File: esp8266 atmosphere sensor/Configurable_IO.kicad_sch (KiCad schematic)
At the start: 5 parts, among them J14 Conn_01x03

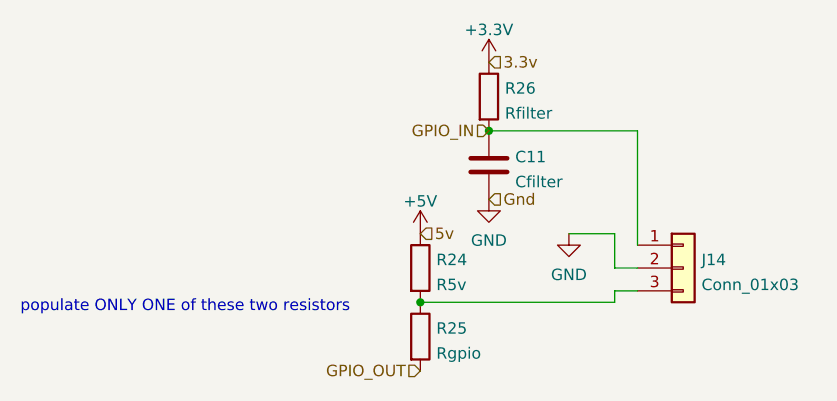
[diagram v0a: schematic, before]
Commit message: updated footprints
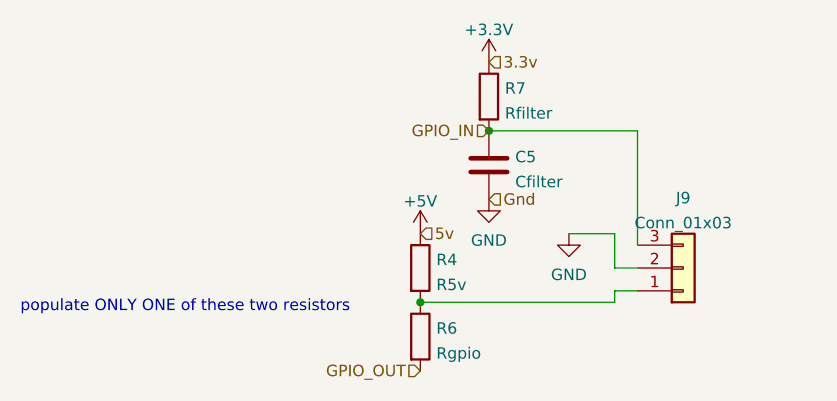
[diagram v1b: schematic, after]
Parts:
- renumbered C11 to C5, J14 to J9, R24 to R4, R25 to R6, R26 to R7
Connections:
- net GPIO_IN: now also J9.3 (Pin_3); no longer J9.1 (Pin_1)
- net at R4.2, R6.1: now also J9.1 (Pin_1); no longer J9.3 (Pin_3)
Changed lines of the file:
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@@
   (symbol (lib_id "power:GND") (at 82.55 60.96 0)
     (in_bom yes) (on_board yes) (fields_autoplaced)
-    (property "Reference" "#PWR0171" (id 0) (at 82.55 67.31 0)
+    (property "Reference" "#PWR0151" (id 0) (at 82.55 67.31 0)
       (effects (font (size 1.27 1.27)) hide)
     )
@@
   (symbol (lib_id "Device:R") (at 74.93 68.58 0)
     (in_bom yes) (on_board yes) (fields_autoplaced)
-    (property "Reference" "R24" (id 0) (at 76.708 67.6715 0)
+    (property "Reference" "R4" (id 0) (at 76.708 67.6715 0)
       (effects (font (size 1.27 1.27)) (justify left))
     )
@@
     (pin "2")
   )
-  (symbol (lib_id "Connector_Generic:Conn_01x03") (at 104.14 68.58 0)
+  (symbol (lib_id "Connector_Generic:Conn_01x03") (at 104.14 68.58 0) (mirror x)
     (in_bom yes) (on_board yes) (fields_autoplaced)
-    (property "Reference" "J14" (id 0) (at 106.172 67.6715 0)
-      (effects (font (size 1.27 1.27)) (justify left))
-    )
-    (property "Value" "Conn_01x03" (id 1) (at 106.172 70.4466 0)
-      (effects (font (size 1.27 1.27)) (justify left))
-    )
+    (property "Reference" "J9" (id 0) (at 104.14 60.8035 0))
+    (property "Value" "Conn_01x03" (id 1) (at 104.14 63.5786 0))
     (property "Footprint" "Connector_JST:JST_PH_B3B-PH-SM4-TB_1x03-1MP_P2.00mm_Vertical" (id 2) (at 104.14 68.58 0)
       (effects (font (size 1.27 1.27)) hide)
@@
   (symbol (lib_id "power:GND") (at 91.44 64.77 0)
     (in_bom yes) (on_board yes) (fields_autoplaced)
-    (property "Reference" "#PWR0174" (id 0) (at 91.44 71.12 0)
+    (property "Reference" "#PWR0154" (id 0) (at 91.44 71.12 0)
       (effects (font (size 1.27 1.27)) hide)
     )
@@
   (symbol (lib_id "power:+3.3V") (at 82.55 45.72 0)
     (in_bom yes) (on_board yes) (fields_autoplaced)
-    (property "Reference" "#PWR0173" (id 0) (at 82.55 49.53 0)
+    (property "Reference" "#PWR0153" (id 0) (at 82.55 49.53 0)
       (effects (font (size 1.27 1.27)) hide)
     )
@@
   (symbol (lib_id "Device:C") (at 82.55 57.15 0)
     (in_bom yes) (on_board yes) (fields_autoplaced)
-    (property "Reference" "C11" (id 0) (at 85.471 56.2415 0)
+    (property "Reference" "C5" (id 0) (at 85.471 56.2415 0)
       (effects (font (size 1.27 1.27)) (justify left))
     )
@@
   (symbol (lib_id "power:+5V") (at 74.93 64.77 0)
     (in_bom yes) (on_board yes) (fields_autoplaced)
-    (property "Reference" "#PWR0172" (id 0) (at 74.93 68.58 0)
+    (property "Reference" "#PWR0152" (id 0) (at 74.93 68.58 0)
       (effects (font (size 1.27 1.27)) hide)
     )
@@
   (symbol (lib_id "Device:R") (at 82.55 49.53 0)
     (in_bom yes) (on_board yes) (fields_autoplaced)
-    (property "Reference" "R26" (id 0) (at 84.328 48.6215 0)
+    (property "Reference" "R7" (id 0) (at 84.328 48.6215 0)
       (effects (font (size 1.27 1.27)) (justify left))
     )
@@
   (symbol (lib_id "Device:R") (at 74.93 76.2 0)
     (in_bom yes) (on_board yes) (fields_autoplaced)
-    (property "Reference" "R25" (id 0) (at 76.708 75.2915 0)
+    (property "Reference" "R6" (id 0) (at 76.708 75.2915 0)
       (effects (font (size 1.27 1.27)) (justify left))
     )

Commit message: added notes for populating switch components
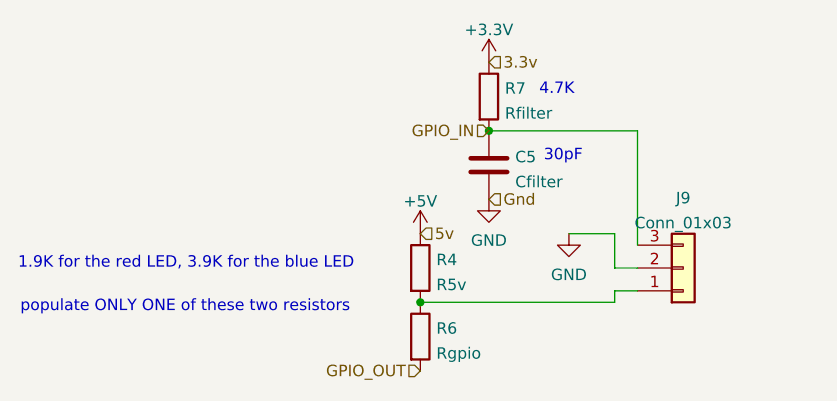
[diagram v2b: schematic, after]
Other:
- note added: "1.9K for the red LED, 3.9K for the blue LED"
- note added: "30pF"
- note added: "4.7K"
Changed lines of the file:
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@@
     (stroke (width 0) (type default) (color 0 0 0 0))
+  )
+  (text "4.7K" (at 88.138 49.53 0)
+    (effects (font (size 1.27 1.27)) (justify left bottom))
+  )
+  (text "1.9K for the red LED, 3.9K for the blue LED" (at 30.226 68.834 0)
+    (effects (font (size 1.27 1.27)) (justify left bottom))
+  )
+  (text "30pF" (at 88.646 56.896 0)
+    (effects (font (size 1.27 1.27)) (justify left bottom))
   )
   (text "populate ONLY ONE of these two resistors" (at 30.48 73.66 0)
@@
     (effects (font (size 1.27 1.27)) (justify left))
   )
-  (symbol (lib_id "power:GND") (at 82.55 60.96 0)
+  (symbol (lib_id "power:GND") (at 82.55 60.96 0) (unit 1)
     (in_bom yes) (on_board yes) (fields_autoplaced)
     (property "Reference" "#PWR0151" (id 0) (at 82.55 67.31 0)
@@
     (pin "1")
   )
-  (symbol (lib_id "Device:R") (at 74.93 68.58 0)
+  (symbol (lib_id "Device:R") (at 74.93 68.58 0) (unit 1)
     (in_bom yes) (on_board yes) (fields_autoplaced)
     (property "Reference" "R4" (id 0) (at 76.708 67.6715 0)
@@
     (pin "2")
   )
-  (symbol (lib_id "Connector_Generic:Conn_01x03") (at 104.14 68.58 0) (mirror x)
+  (symbol (lib_id "Connector_Generic:Conn_01x03") (at 104.14 68.58 0) (mirror x) (unit 1)
     (in_bom yes) (on_board yes) (fields_autoplaced)
     (property "Reference" "J9" (id 0) (at 104.14 60.8035 0))
@@
     (pin "3")
   )
-  (symbol (lib_id "power:GND") (at 91.44 64.77 0)
+  (symbol (lib_id "power:GND") (at 91.44 64.77 0) (unit 1)
     (in_bom yes) (on_board yes) (fields_autoplaced)
     (property "Reference" "#PWR0154" (id 0) (at 91.44 71.12 0)
@@
     (pin "1")
   )
-  (symbol (lib_id "power:+3.3V") (at 82.55 45.72 0)
+  (symbol (lib_id "power:+3.3V") (at 82.55 45.72 0) (unit 1)
     (in_bom yes) (on_board yes) (fields_autoplaced)
     (property "Reference" "#PWR0153" (id 0) (at 82.55 49.53 0)
@@
     (pin "1")
   )
-  (symbol (lib_id "Device:C") (at 82.55 57.15 0)
+  (symbol (lib_id "Device:C") (at 82.55 57.15 0) (unit 1)
     (in_bom yes) (on_board yes) (fields_autoplaced)
     (property "Reference" "C5" (id 0) (at 85.471 56.2415 0)
@@
     (pin "2")
   )
-  (symbol (lib_id "power:+5V") (at 74.93 64.77 0)
+  (symbol (lib_id "power:+5V") (at 74.93 64.77 0) (unit 1)
     (in_bom yes) (on_board yes) (fields_autoplaced)
     (property "Reference" "#PWR0152" (id 0) (at 74.93 68.58 0)
@@
     (pin "1")
   )
-  (symbol (lib_id "Device:R") (at 82.55 49.53 0)
+  (symbol (lib_id "Device:R") (at 82.55 49.53 0) (unit 1)
     (in_bom yes) (on_board yes) (fields_autoplaced)
     (property "Reference" "R7" (id 0) (at 84.328 48.6215 0)
@@
     (pin "2")
   )
-  (symbol (lib_id "Device:R") (at 74.93 76.2 0)
+  (symbol (lib_id "Device:R") (at 74.93 76.2 0) (unit 1)
     (in_bom yes) (on_board yes) (fields_autoplaced)
     (property "Reference" "R6" (id 0) (at 76.708 75.2915 0)

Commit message: tweaked locations for button connectors
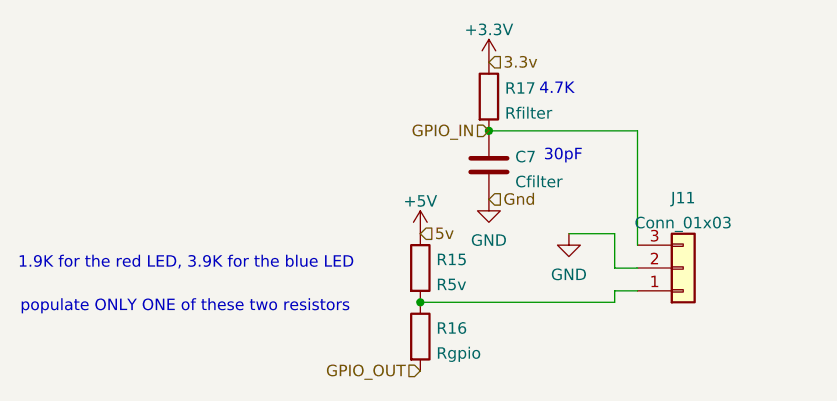
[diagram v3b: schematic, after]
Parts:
- renumbered C5 to C7, J9 to J11, R4 to R15, R6 to R16, R7 to R17
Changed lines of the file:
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@@
     (effects (font (size 1.27 1.27)) (justify left))
   )
-  (symbol (lib_id "power:GND") (at 82.55 60.96 0) (unit 1)
+  (symbol (lib_id "power:GND") (at 82.55 60.96 0)
     (in_bom yes) (on_board yes) (fields_autoplaced)
-    (property "Reference" "#PWR0151" (id 0) (at 82.55 67.31 0)
+    (property "Reference" "#PWR0159" (id 0) (at 82.55 67.31 0)
       (effects (font (size 1.27 1.27)) hide)
     )
@@
     (pin "1")
   )
-  (symbol (lib_id "Device:R") (at 74.93 68.58 0) (unit 1)
+  (symbol (lib_id "Device:R") (at 74.93 68.58 0)
     (in_bom yes) (on_board yes) (fields_autoplaced)
-    (property "Reference" "R4" (id 0) (at 76.708 67.6715 0)
+    (property "Reference" "R15" (id 0) (at 76.708 67.6715 0)
       (effects (font (size 1.27 1.27)) (justify left))
     )
@@
     (pin "2")
   )
-  (symbol (lib_id "Connector_Generic:Conn_01x03") (at 104.14 68.58 0) (mirror x) (unit 1)
+  (symbol (lib_id "Connector_Generic:Conn_01x03") (at 104.14 68.58 0) (mirror x)
     (in_bom yes) (on_board yes) (fields_autoplaced)
-    (property "Reference" "J9" (id 0) (at 104.14 60.8035 0))
+    (property "Reference" "J11" (id 0) (at 104.14 60.8035 0))
     (property "Value" "Conn_01x03" (id 1) (at 104.14 63.5786 0))
     (property "Footprint" "Connector_JST:JST_PH_B3B-PH-SM4-TB_1x03-1MP_P2.00mm_Vertical" (id 2) (at 104.14 68.58 0)
@@
     (pin "3")
   )
-  (symbol (lib_id "power:GND") (at 91.44 64.77 0) (unit 1)
+  (symbol (lib_id "power:GND") (at 91.44 64.77 0)
     (in_bom yes) (on_board yes) (fields_autoplaced)
-    (property "Reference" "#PWR0154" (id 0) (at 91.44 71.12 0)
+    (property "Reference" "#PWR0162" (id 0) (at 91.44 71.12 0)
       (effects (font (size 1.27 1.27)) hide)
     )
@@
     (pin "1")
   )
-  (symbol (lib_id "power:+3.3V") (at 82.55 45.72 0) (unit 1)
+  (symbol (lib_id "power:+3.3V") (at 82.55 45.72 0)
     (in_bom yes) (on_board yes) (fields_autoplaced)
-    (property "Reference" "#PWR0153" (id 0) (at 82.55 49.53 0)
+    (property "Reference" "#PWR0161" (id 0) (at 82.55 49.53 0)
       (effects (font (size 1.27 1.27)) hide)
     )
@@
     (pin "1")
   )
-  (symbol (lib_id "Device:C") (at 82.55 57.15 0) (unit 1)
+  (symbol (lib_id "Device:C") (at 82.55 57.15 0)
     (in_bom yes) (on_board yes) (fields_autoplaced)
-    (property "Reference" "C5" (id 0) (at 85.471 56.2415 0)
+    (property "Reference" "C7" (id 0) (at 85.471 56.2415 0)
       (effects (font (size 1.27 1.27)) (justify left))
     )
@@
     (pin "2")
   )
-  (symbol (lib_id "power:+5V") (at 74.93 64.77 0) (unit 1)
+  (symbol (lib_id "power:+5V") (at 74.93 64.77 0)
     (in_bom yes) (on_board yes) (fields_autoplaced)
-    (property "Reference" "#PWR0152" (id 0) (at 74.93 68.58 0)
+    (property "Reference" "#PWR0160" (id 0) (at 74.93 68.58 0)
       (effects (font (size 1.27 1.27)) hide)
     )
@@
     (pin "1")
   )
-  (symbol (lib_id "Device:R") (at 82.55 49.53 0) (unit 1)
+  (symbol (lib_id "Device:R") (at 82.55 49.53 0)
     (in_bom yes) (on_board yes) (fields_autoplaced)
-    (property "Reference" "R7" (id 0) (at 84.328 48.6215 0)
+    (property "Reference" "R17" (id 0) (at 84.328 48.6215 0)
       (effects (font (size 1.27 1.27)) (justify left))
     )
@@
     (pin "2")
   )
-  (symbol (lib_id "Device:R") (at 74.93 76.2 0) (unit 1)
+  (symbol (lib_id "Device:R") (at 74.93 76.2 0)
     (in_bom yes) (on_board yes) (fields_autoplaced)
-    (property "Reference" "R6" (id 0) (at 76.708 75.2915 0)
+    (property "Reference" "R16" (id 0) (at 76.708 75.2915 0)
       (effects (font (size 1.27 1.27)) (justify left))
     )
